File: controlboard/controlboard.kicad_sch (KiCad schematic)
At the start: 32 parts, among them J10 Conn_01x02_Pin, J27 GPIO, J6 Conn_02x04_Counter_Clockwise, SW2 SW_Push TODO FP CHECK

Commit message: improvements
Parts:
- removed J10: Conn_01x02_Pin, symbol Connector:Conn_01x02_Pin
- TP15: footprint (none) -> Connector_PinSocket_2.54mm:PinSocket_1x01_P2.54mm_Vertical
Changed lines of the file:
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@@
 	)
 	(junction
-		(at 176.53 66.04)
-		(diameter 0)
-		(color 0 0 0 0)
-	)
-	(junction
 		(at 100.33 45.72)
 		(diameter 1.016)
@@
 		(color 0 0 0 0)
 	)
-	(junction
-		(at 176.53 55.88)
-		(diameter 0)
-		(color 0 0 0 0)
-	)
 	(no_connect
 		(at 74.93 105.41)
@@
 	(wire
 		(pts
-			(xy 184.15 62.23) (xy 184.15 66.04)
-		)
-		(stroke
-			(width 0)
-			(type default)
-		)
-	)
-	(wire
-		(pts
 			(xy 163.83 140.97) (xy 170.18 140.97)
 		)
@@
 	(wire
 		(pts
-			(xy 184.15 55.88) (xy 176.53 55.88)
-		)
-		(stroke
-			(width 0)
-			(type default)
-		)
-	)
-	(wire
-		(pts
 			(xy 82.55 53.34) (xy 85.09 53.34)
 		)
@@
 	(wire
 		(pts
-			(xy 184.15 59.69) (xy 184.15 55.88)
-		)
-		(stroke
-			(width 0)
-			(type default)
-		)
-	)
-	(wire
-		(pts
 			(xy 48.26 58.42) (xy 85.09 58.42)
 		)
@@
 	(wire
 		(pts
-			(xy 184.15 66.04) (xy 176.53 66.04)
-		)
-		(stroke
-			(width 0)
-			(type default)
-		)
-	)
-	(wire
-		(pts
 			(xy 190.5 87.63) (xy 180.34 87.63)
 		)
@@
 				)
 				(justify right)
+				(hide yes)
 			)
 		)
@@
 			)
 		)
-		(property "Footprint" ""
+		(property "Footprint" "Connector_PinSocket_2.54mm:PinSocket_1x01_P2.54mm_Vertical"
 			(at 276.86 139.7 0)
 			(effects
@@
 					(unit 1)
 				)
-			)
-		)
-	)
-	(symbol
-		(lib_id "Connector:Conn_01x02_Pin")
-		(at 189.23 62.23 180)
-		(unit 1)
-		(exclude_from_sim no)
-		(in_bom yes)
-		(on_board yes)
-		(dnp no)
-		(fields_autoplaced yes)
-		(property "Reference" "J10"
-			(at 190.5 59.6899 0)
-			(effects
-				(font
-					(size 1.27 1.27)
-				)
-				(justify right)
-			)
-		)
-		(property "Value" "Conn_01x02_Pin"
-			(at 190.5 62.2299 0)
-			(effects
-				(font
-					(size 1.27 1.27)
-				)
-				(justify right)
-			)
-		)
-		(property "Footprint" ""
-			(at 189.23 62.23 0)
-			(effects
-				(font
-					(size 1.27 1.27)
-				)
-				(hide yes)
-			)
-		)
-		(property "Datasheet" "~"
-			(at 189.23 62.23 0)
-			(effects
-				(font
-					(size 1.27 1.27)
-				)
-				(hide yes)
-			)
-		)
-		(property "Description" "Generic connector, single row, 01x02, script generated"
-			(at 189.23 62.23 0)
-			(effects
-				(font
-					(size 1.27 1.27)
-				)
-				(hide yes)
-			)
-		)
-		(pin "1"
-		)
-		(pin "2"
-		)
-		(instances
-			(project "controlboard"
-				(path "/2797250d-6fee-4769-b4dd-0e20ce4f0941"
-					(reference "J10")
-					(unit 1)
-				)

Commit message: erc should be good now
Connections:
- net GPIO10/SPI0.MOSI renamed LCD/TP_SI
- net GPIO11/SPI0.SCLK renamed LED/TP_SCK
- net GPIO12/PWM0 renamed LED_DATA
- net GPIO13/PWM1: no longer names the net of J27.33 (Pin_33), R60.2
- net GPIO14/TXD0: no longer names the net of J27.8 (Pin_8), R16.1
- net GPIO15/RXD0: no longer names the net of J27.10 (Pin_10), R17.1
- net GPIO16: no longer names the net of J27.36 (Pin_36), R52.1
- net GPIO17 renamed TP_IRQ
- net GPIO18/PCM.CLK: no longer names the net of J27.12 (Pin_12), R18.1
- net GPIO19/PCM.FS: no longer names the net of J27.35 (Pin_35), R61.2
- net GPIO20/PCM.DIN: no longer names the net of J27.38 (Pin_38), R53.1
- net GPIO21/PCM.DOUT: no longer names the net of J27.40 (Pin_40), R54.1
- net GPIO22: no longer names the net of J27.15 (Pin_15), R64.2
- net GPIO23: no longer names the net of J27.16 (Pin_16), R65.1
- net GPIO24 renamed LCD_RS
- net GPIO25 renamed LCD_RST
- net GPIO26: no longer names the net of J27.37 (Pin_37), R62.2
- net GPIO27: no longer names the net of J27.13 (Pin_13), R63.2
- net GPIO2/SDA1: no longer names the net of J27.3 (Pin_3), R67.2
- net GPIO3/SCL1: no longer names the net of J27.5 (Pin_5), R68.2
- net GPIO4/GPCLK0: no longer names the net of J27.7 (Pin_7), R66.2
- net GPIO5: no longer names the net of J27.29 (Pin_29), R55.2
- net GPIO6: no longer names the net of J27.31 (Pin_31), R56.2
- net GPIO7/SPI0.CE1 renamed TP_CS
- net GPIO8/SPI0.CE0 renamed LCD_CS
- net GPIO9/SPI0.MISO renamed TP_SO
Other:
- note added: "GPIO10/SPI0.MOSI"
- note added: "GPIO11/SPI0.SCLK"
- note added: "GPIO12/PWM0"
- note added: "GPIO13/PWM1"
- note added: "GPIO14/TXD0"
- note added: "GPIO15/RXD0"
- note added: "GPIO16"
- note added: "GPIO17"
- note added: "GPIO18/PCM.CLK"
- note added: "GPIO19/PCM.FS"
- note added: "GPIO2/SDA1"
- note added: "GPIO20/PCM.DIN"
- note added: "GPIO21/PCM.DOUT"
- note added: "GPIO22"
- note added: "GPIO23"
- note added: "GPIO24"
- note added: "GPIO25"
- note added: "GPIO26"
- note added: "GPIO27"
- note added: "GPIO3/SCL1"
- note added: "GPIO4/GPCLK0"
- note added: "GPIO5"
- note added: "GPIO6"
- note added: "GPIO7/SPI0.CE1"
- note added: "GPIO8/SPI0.CE0"
- note added: "GPIO9/SPI0.MISO"

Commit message: pcb layout work
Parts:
- J27: footprint Connector_PinSocket_2.54mm:PinSocket_2x20_P2.54mm_Vertical_SMD -> Connector_Samtec_HLE_SMD:Samtec_HLE-120-02-xxx-DV-BE-A_2x20_P2.54mm_Horizontal; LCSC (none) -> C2685112
- JP13, JP14, JP15, JP16, JP17: footprint TestPoint:TestPoint_2Pads_Pitch2.54mm_Drill0.8mm -> 0chessbot-parts:Bridged_TestPoint_2Pads_Pitch2.54mm_Drill0.8mm
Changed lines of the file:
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@@
 			)
 		)
-		(property "Footprint" "TestPoint:TestPoint_2Pads_Pitch2.54mm_Drill0.8mm"
+		(property "Footprint" "0chessbot-parts:Bridged_TestPoint_2Pads_Pitch2.54mm_Drill0.8mm"
 			(at 158.75 146.05 0)
 			(effects
@@
 			)
 		)
-		(property "Footprint" "TestPoint:TestPoint_2Pads_Pitch2.54mm_Drill0.8mm"
+		(property "Footprint" "0chessbot-parts:Bridged_TestPoint_2Pads_Pitch2.54mm_Drill0.8mm"
 			(at 158.75 135.89 0)
 			(effects
@@
 			)
 		)
-		(property "Footprint" "Connector_PinSocket_2.54mm:PinSocket_2x20_P2.54mm_Vertical_SMD"
+		(property "Footprint" "Connector_Samtec_HLE_SMD:Samtec_HLE-120-02-xxx-DV-BE-A_2x20_P2.54mm_Horizontal"
 			(at -33.02 69.85 0)
 			(effects
@@
 			)
 		)
+		(property "LCSC" "C2685112"
+			(at 90.17 45.72 0)
+			(effects
+				(font
+					(size 1.27 1.27)
+				)
+				(hide yes)
+			)
+		)
 		(pin "1"
 		)
@@
 			)
 		)
-		(property "Footprint" "TestPoint:TestPoint_2Pads_Pitch2.54mm_Drill0.8mm"
+		(property "Footprint" "0chessbot-parts:Bridged_TestPoint_2Pads_Pitch2.54mm_Drill0.8mm"
 			(at 158.75 138.43 0)
 			(effects
@@
 			)
 		)
-		(property "Footprint" "TestPoint:TestPoint_2Pads_Pitch2.54mm_Drill0.8mm"
+		(property "Footprint" "0chessbot-parts:Bridged_TestPoint_2Pads_Pitch2.54mm_Drill0.8mm"
 			(at 158.75 143.51 0)
 			(effects
@@
 			)
 		)
-		(property "Footprint" "TestPoint:TestPoint_2Pads_Pitch2.54mm_Drill0.8mm"
+		(property "Footprint" "0chessbot-parts:Bridged_TestPoint_2Pads_Pitch2.54mm_Drill0.8mm"
 			(at 158.75 140.97 0)
 			(effects

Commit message: progress
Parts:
- added R10, R11, R9: 1k, Resistor_SMD:R_0603_1608Metric_Pad0.98x0.95mm_HandSolder, symbol Device:R
- J6: symbol Connector_Generic:Conn_02x04_Counter_Clockwise -> Connector_Generic:Conn_02x04_Odd_Even
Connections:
- net CH_5V: now also J6.4 (Pin_4); no longer J6.7 (Pin_7)
- net DIR1: now also R65.1; no longer R16.2
- net GND: now also J6.6 (Pin_6); no longer J6.2 (Pin_2)
- net ID_SCL: now also J6.5 (Pin_5), R10.2; no longer J6.3 (Pin_3), R69.2
- net ID_SDA: now also J6.3 (Pin_3), R9.1; no longer J6.4 (Pin_4), R70.1
- net LED_DATA: now also R11.2; no longer J27.32 (Pin_32)
- net LIM_SW1: now also R66.1; no longer R63.1
- net LIM_SW2: now also R16.2; no longer R64.1
- net LIM_SW3: now also R17.2; no longer R65.2
- net LIM_SW4: now also R64.1; no longer R66.1
- net PI_5V: no longer J6.6 (Pin_6)
- net Power/PWR_SW_A: now also J6.2 (Pin_2); no longer J6.8 (Pin_8)
- net Power/VMOT: now also J6.8 (Pin_8); no longer J6.5 (Pin_5)
- net STEP1: now also R63.1; no longer R17.2
- net at J27.16 (Pin_16): now also R65.2; no longer R65.1
- new net: R70.1, R9.2
- new net: R10.1, R69.2
- new net: J27.32 (Pin_32), R11.1
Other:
- moved on the sheet: R65

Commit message: yay its all connected
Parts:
- TP15: footprint Connector_PinSocket_2.54mm:PinSocket_1x01_P2.54mm_Vertical -> TestPoint:TestPoint_THTPad_D2.0mm_Drill1.0mm
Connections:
- net PI_3V3: no longer J27.1 (Pin_1)
- no-connect marks 1 -> 2
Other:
- note added: "PI_3V3_secondary"
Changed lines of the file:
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@@
 	(paper "A4")
 	(junction
-		(at 80.01 22.86)
-		(diameter 1.016)
-		(color 0 0 0 0)
-	)
-	(junction
 		(at 100.33 58.42)
 		(diameter 1.016)
@@
 		(at 74.93 105.41)
 	)
+	(no_connect
+		(at 85.09 22.86)
+	)
 	(wire
 		(pts
@@
 	(wire
 		(pts
-			(xy 80.01 22.86) (xy 80.01 43.18)
-		)
-		(stroke
-			(width 0)
-			(type solid)
-		)
-	)
-	(wire
-		(pts
 			(xy 163.83 146.05) (xy 170.18 146.05)
 		)
@@
 	(wire
 		(pts
-			(xy 80.01 22.86) (xy 85.09 22.86)
-		)
-		(stroke
-			(width 0)
-			(type solid)
-		)
-	)
-	(wire
-		(pts
 			(xy 238.76 135.89) (xy 241.3 135.89)
 		)
@@
 	(wire
 		(pts
-			(xy 80.01 19.05) (xy 80.01 22.86)
-		)
-		(stroke
-			(width 0)
-			(type solid)
-		)
-	)
-	(wire
-		(pts
 			(xy 85.09 55.88) (xy 74.93 55.88)
 		)
@@
 		)
 	)
+	(text "PI_3V3_secondary"
+		(exclude_from_sim no)
+		(at 75.946 22.86 0)
+		(effects
+			(font
+				(size 1.27 1.27)
+			)
+		)
+	)
 	(text "GPIO17"
 		(exclude_from_sim no)
@@
 	)
 	(label "PI_3V3"
-		(at 80.01 19.05 180)
+		(at 80.01 43.18 180)
 		(fields_autoplaced yes)
 		(effects
@@
 			)
 		)
-		(property "Footprint" "Connector_PinSocket_2.54mm:PinSocket_1x01_P2.54mm_Vertical"
+		(property "Footprint" "TestPoint:TestPoint_THTPad_D2.0mm_Drill1.0mm"
 			(at 276.86 139.7 0)
 			(effects

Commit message: a
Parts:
- J27: footprint Connector_Samtec_HLE_SMD:Samtec_HLE-120-02-xxx-DV-BE-A_2x20_P2.54mm_Horizontal -> 0chessbot-parts:Samtec_HLE-120-02-xxx-DV-BE-A_2x20_P2.54mm_Horizontal
- SW2: footprint Button_Switch_SMD:SW_SPST_SKQG_WithStem -> 0chessbot-parts:SW_SPST_SKQG_WithStem
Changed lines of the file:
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@@
 			)
 		)
-		(property "Footprint" "Button_Switch_SMD:SW_SPST_SKQG_WithStem"
+		(property "Footprint" "0chessbot-parts:SW_SPST_SKQG_WithStem"
 			(at 181.61 60.96 0)
 			(effects
@@
 			)
 		)
-		(property "Footprint" "Connector_Samtec_HLE_SMD:Samtec_HLE-120-02-xxx-DV-BE-A_2x20_P2.54mm_Horizontal"
+		(property "Footprint" "0chessbot-parts:Samtec_HLE-120-02-xxx-DV-BE-A_2x20_P2.54mm_Horizontal"
 			(at -33.02 69.85 0)
 			(effects

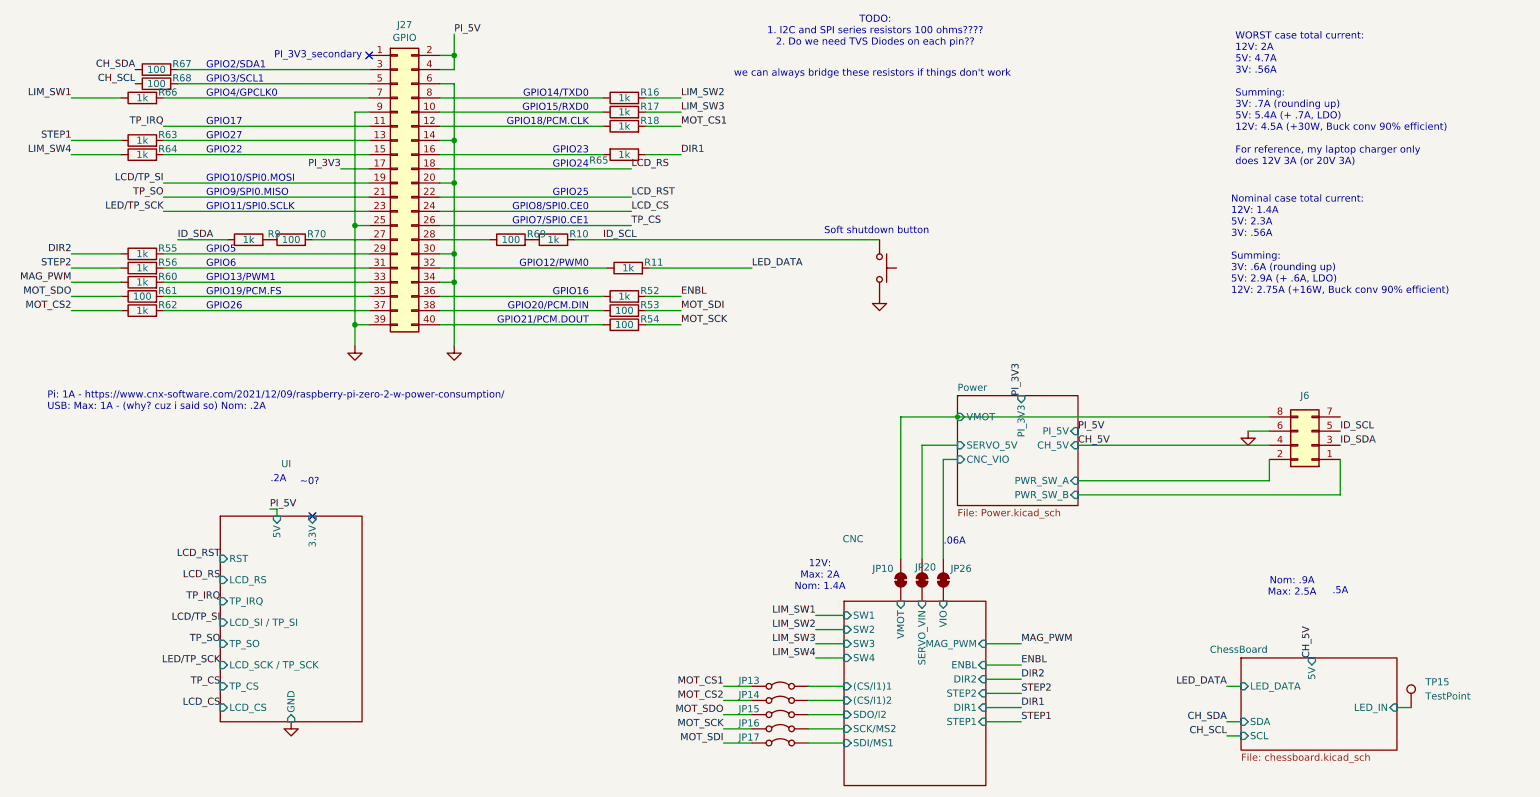
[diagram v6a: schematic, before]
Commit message: controlboard: fix critical mosfet errors
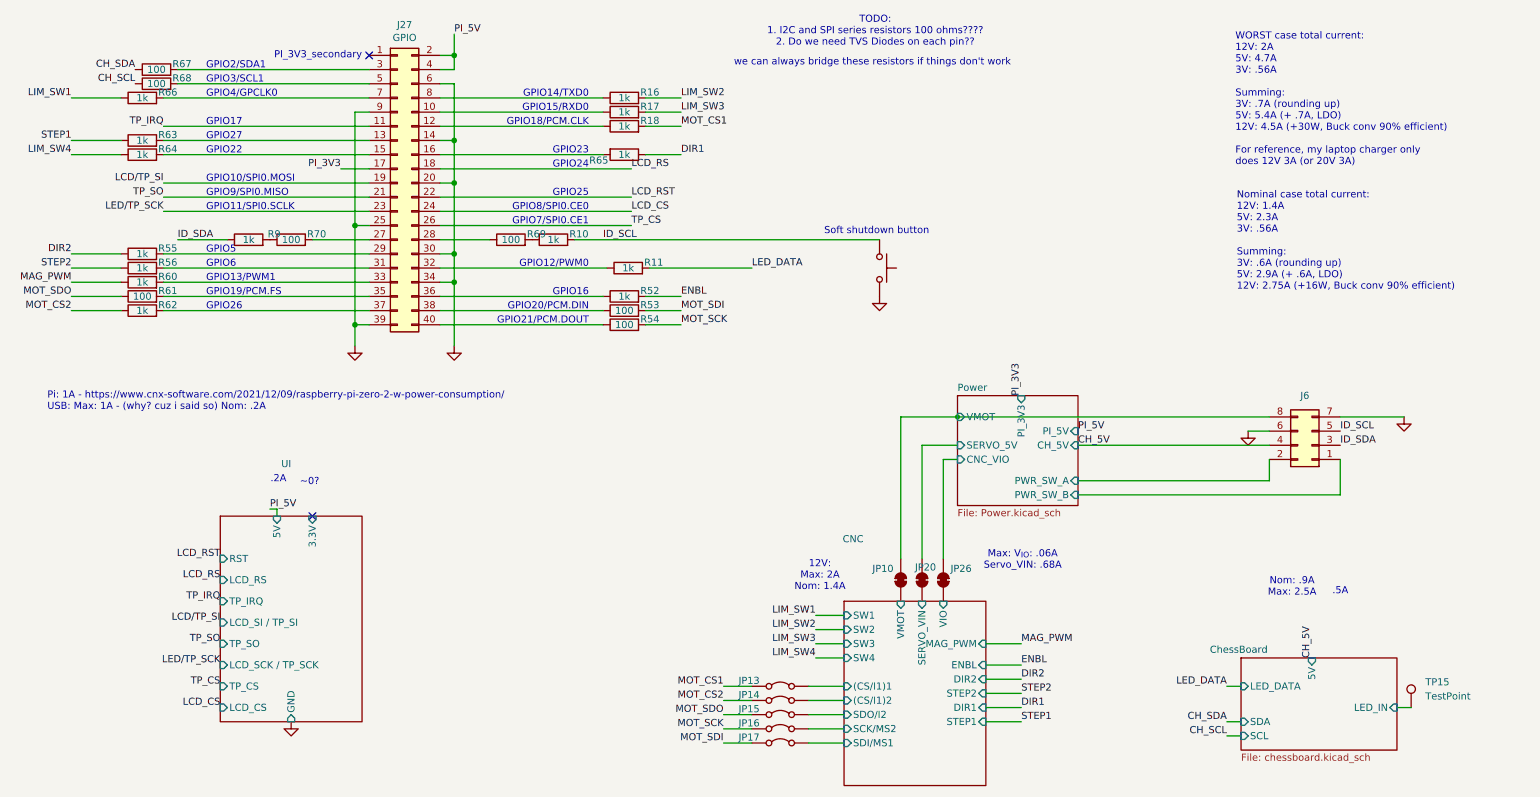
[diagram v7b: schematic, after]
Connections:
- net GND: now also J6.7 (Pin_7)
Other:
- note added: "Max: V_{IO}: .06A Servo_VIN: .68A"
- note removed: ".06A"
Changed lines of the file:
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@@
 	(wire
 		(pts
+			(xy 270.51 87.63) (xy 259.08 87.63)
+		)
+		(stroke
+			(width 0)
+			(type default)
+		)
+	)
+	(wire
+		(pts
 			(xy 100.33 27.94) (xy 97.79 27.94)
 		)
@@
 		)
 	)
-	(text ".06A"
+	(text "GPIO12/PWM0"
 		(exclude_from_sim no)
-		(at 189.992 109.982 0)
+		(at 124.46 60.96 0)
 		(effects
 			(font
 				(size 1.27 1.27)
 			)
+			(justify right bottom)
 		)
 	)
-	(text "GPIO12/PWM0"
+	(text "GPIO15/RXD0"
 		(exclude_from_sim no)
-		(at 124.46 60.96 0)
+		(at 124.46 33.02 0)
 		(effects
 			(font
@@
 		)
 	)
-	(text "GPIO15/RXD0"
+	(text "Max: V_{IO}: .06A\nServo_VIN: .68A"
 		(exclude_from_sim no)
-		(at 124.46 33.02 0)
+		(at 202.184 113.284 0)
 		(effects
 			(font
 				(size 1.27 1.27)
 			)
-			(justify right bottom)
 		)
 	)
@@
 	(text "we can always bridge these resistors if things don't work"
 		(exclude_from_sim no)
-		(at 175.26 26.162 0)
+		(at 175.26 24.13 0)
 		(effects
 			(font
@@
 	(text "Nominal case total current:\n12V: 1.4A\n5V: 2.3A\n3V: .56A\n\nSumming:\n3V: .6A (rounding up)\n5V: 2.9A (+ .6A, LDO)\n12V: 2.75A (+16W, Buck conv 90% efficient)\n"
 		(exclude_from_sim no)
-		(at 239.522 56.896 0)
+		(at 240.538 56.134 0)
 		(effects
 			(font
@@
 					(unit 1)
 				)
+			)
+		)
+	)
+	(symbol
+		(lib_id "power:GND")
+		(at 270.51 87.63 0)
+		(mirror y)
+		(unit 1)
+		(exclude_from_sim no)
+		(in_bom yes)
+		(on_board yes)
+		(dnp no)
+		(property "Reference" "#PWR048"
+			(at 270.51 93.98 0)
+			(effects
+				(font
+					(size 1.27 1.27)
+				)
+				(hide yes)
+			)
+		)
+		(property "Value" "GND"
+			(at 270.3957 91.9544 0)
+			(effects
+				(font
+					(size 1.27 1.27)
+				)
+				(hide yes)
+			)
+		)
+		(property "Footprint" ""
+			(at 270.51 87.63 0)
+			(effects
+				(font
+					(size 1.27 1.27)
+				)
+			)
+		)
+		(property "Datasheet" ""
+			(at 270.51 87.63 0)
+			(effects
+				(font
+					(size 1.27 1.27)
+				)
+			)
+		)
+		(property "Description" "Power symbol creates a global label with name \"GND\" , ground"
+			(at 270.51 87.63 0)
+			(effects
+				(font
+					(size 1.27 1.27)
+				)
+				(hide yes)
+			)
+		)
+		(pin "1"
+		)
+		(instances
+			(project "controlboard"
+				(path "/2797250d-6fee-4769-b4dd-0e20ce4f0941"
+					(reference "#PWR048")
+					(unit 1)
+				)

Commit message: nice silkscreen stuff
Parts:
- J27: now not fitted
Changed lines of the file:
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@@
 		(in_bom yes)
 		(on_board yes)
-		(dnp no)
+		(dnp yes)
 		(property "Reference" "J27"
 			(at 91.44 17.3798 0)
